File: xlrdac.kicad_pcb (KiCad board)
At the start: 2 copper layers, 99 x 99 mm, 19 parts, among them J1 Screw_Terminal_01x01, J2 Right Output, J3 Left Output, J4 Audio Stereo Input, U1 THAT1646, U2 THAT1646

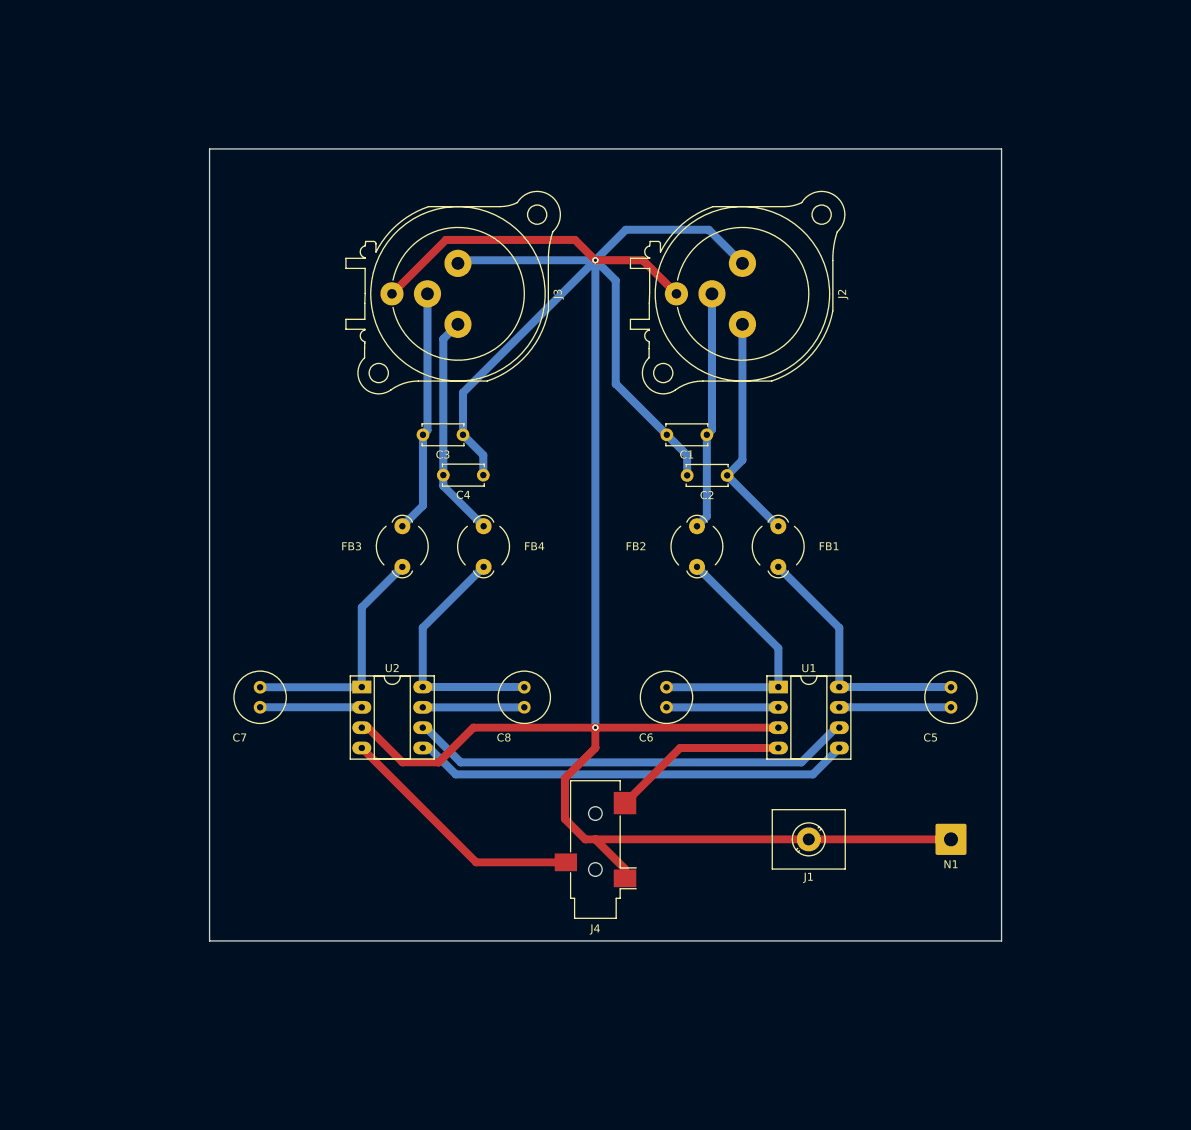
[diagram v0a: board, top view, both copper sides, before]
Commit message: Rework grounding, export side view
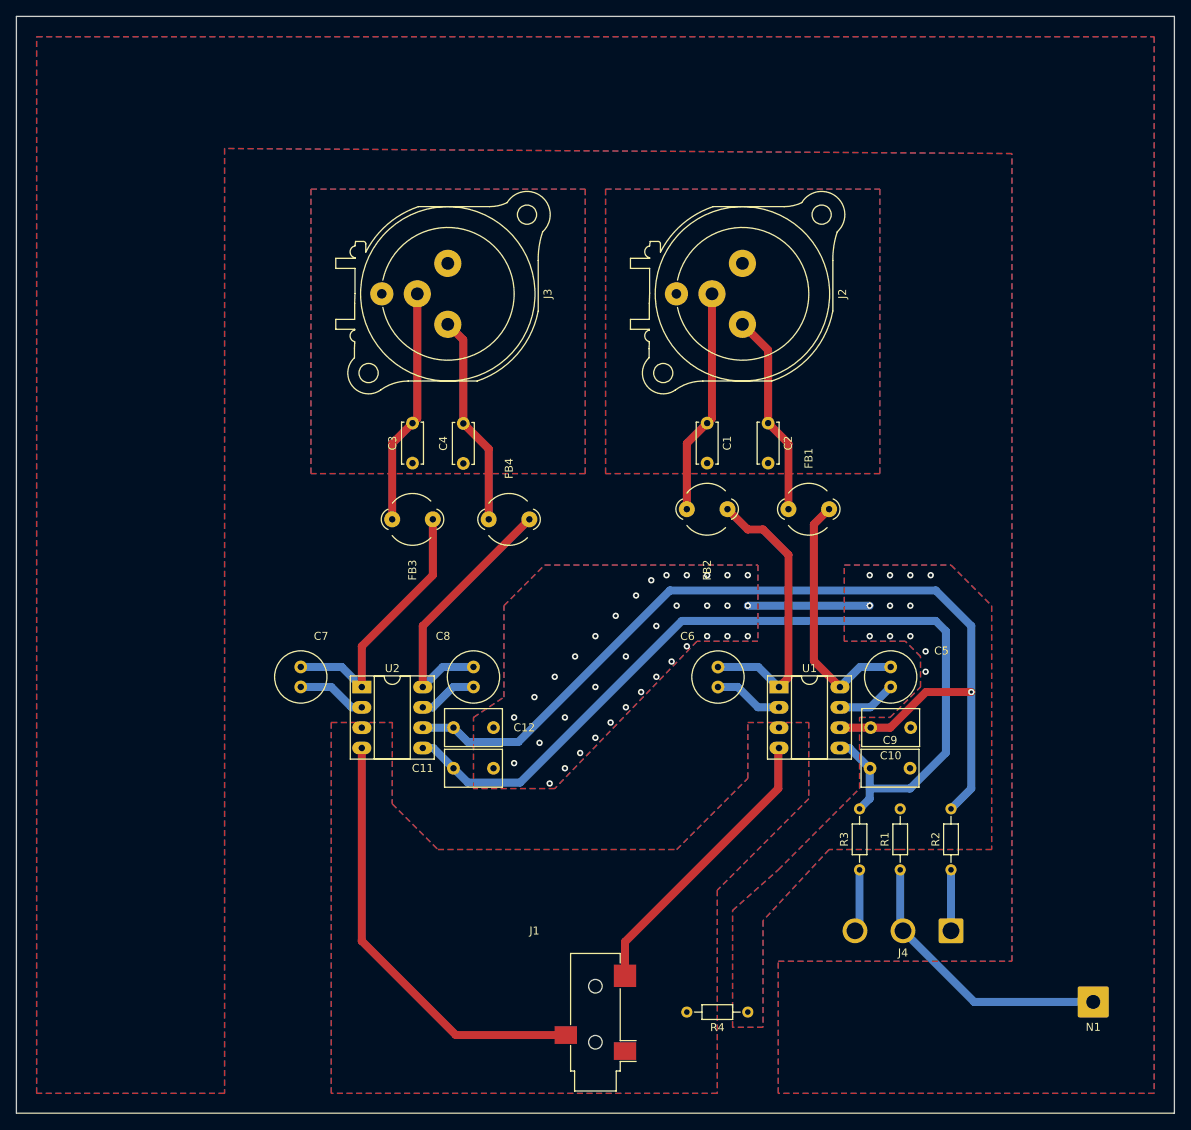
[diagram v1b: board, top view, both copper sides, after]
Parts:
- added C10: 100nF, Capacitor_THT:C_Rect_L7.0mm_W4.5mm_P5.00mm, F.Cu at (137.2, 125.7)
- added C11: 100nF, Capacitor_THT:C_Rect_L7.0mm_W4.5mm_P5.00mm, F.Cu at (80.0, 130.8)
- added C12: 100nF, Capacitor_THT:C_Rect_L7.0mm_W4.5mm_P5.00mm, F.Cu at (85.0, 125.7)
- added C9: 100nF, Capacitor_THT:C_Rect_L7.0mm_W4.5mm_P5.00mm, F.Cu at (132.1, 130.8)
- added R1: 0R, Resistor_THT:R_Axial_DIN0204_L3.6mm_D1.6mm_P7.62mm_Horizontal, F.Cu at (135.9, 143.5)
- added R2: 0R, Resistor_THT:R_Axial_DIN0204_L3.6mm_D1.6mm_P7.62mm_Horizontal, F.Cu at (142.2, 143.5)
- added R3: 0R, Resistor_THT:R_Axial_DIN0204_L3.6mm_D1.6mm_P7.62mm_Horizontal, F.Cu at (130.8, 143.5)
- added R4: 0R, Resistor_THT:R_Axial_DIN0204_L3.6mm_D1.6mm_P7.62mm_Horizontal, F.Cu at (116.8, 161.3)
- J1: value Screw_Terminal_01x01 -> StereoIn; footprint TerminalBlock_MetzConnect:TerminalBlock_MetzConnect_360271_1x01_Horizontal_ScrewM3.0_Boxed -> Connector_Audio:Jack_3.5mm_CUI_SJ-3523-SMT_Horizontal
- J2: value Right Output -> Left Output
- J3: value Left Output -> Right Output
- J4: value Audio Stereo Input -> PWR ENTRY; footprint Connector_Audio:Jack_3.5mm_CUI_SJ-3523-SMT_Horizontal -> Connector_Wire:SolderWire-1.5sqmm_1x03_P6mm_D1.7mm_OD3mm
- N1: value Housing_Pad -> CASE SHIELD
- moved J4 45.6 mm to (142.2, 151.1)
- moved J1 35.1 mm to (97.8, 162.6)
- moved N1 27.0 mm to (160.0, 160.0)
- moved FB1 9.61 mm to (127.0, 98.4), turned to 180 degrees
- moved C2 8.31 mm to (119.4, 87.7), turned to -90 degrees
- moved FB4 8.25 mm to (89.5, 99.7), turned to 180 degrees
- moved FB2 8.16 mm to (114.3, 98.4), turned to 180 degrees
- moved C5 7.96 mm to (134.7, 120.7)
- moved C3 7.24 mm to (74.9, 92.7), turned to 90 degrees
- moved FB3 7.06 mm to (77.5, 99.7), turned to 180 degrees
- moved C6 6.91 mm to (113.1, 120.7)
- moved C8 6.84 mm to (82.5, 120.7)
- moved C7 5.68 mm to (61.0, 120.7)
- moved C4 2.90 mm to (81.3, 92.7), turned to 90 degrees
- moved C1 1.46 mm to (111.8, 87.7), turned to -90 degrees
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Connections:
- C1 pad 2: Earth_Clean -> Net-(C1-Pad2)
- C2 pad 2: Earth_Clean -> Net-(C1-Pad2)
- C3 pad 1: Earth_Clean -> Net-(C3-Pad1)
- C4 pad 1: Earth_Clean -> Net-(C3-Pad1)
- J2 pad 1: Earth_Clean -> Net-(C1-Pad2)
- J2 pad G: Earth_Clean -> Net-(C1-Pad2)
- J3 pad 1: Earth_Clean -> Net-(C3-Pad1)
- J3 pad G: Earth_Clean -> Net-(C3-Pad1)
- N1 pad 1: Earth_Clean -> PWR.GND
- U1 pad 3: Earth_Clean -> GNDA
- U1 pad 4: Net-(J4-PadT) -> Net-(J1-PadT)
- U2 pad 3: Earth_Clean -> GNDA
- U2 pad 4: Net-(U2-Pad4) -> Net-(J1-PadR)
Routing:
- net Earth_Clean: track 329.4 -> 0.00 mm, vias 2 -> 0
- net VCC: track 55.7 -> 121.2 mm, vias 0 -> 1
- net VEE: track 54.8 -> 113.1 mm
- net Net-(J1-PadR): track 0.00 -> 54.5 mm
- net Net-(J1-PadT): track 0.00 -> 36.4 mm
- net PWR.GND: track 0.00 -> 35.2 mm
- net Net-(U2-Pad4): track 31.4 -> 0.00 mm
- net Net-(J4-PadT): track 22.0 -> 0.00 mm
- net GNDPWR: track 0.00 -> 15.2 mm, vias 0 -> 48
- net PWR.VEE: track 0.00 -> 7.86 mm
- net Net-(C5-Pad1): track 14.0 -> 7.40 mm
- net PWR.VCC: track 0.00 -> 6.35 mm
- net Net-(C8-Pad1): track 12.7 -> 7.40 mm
- net Net-(C6-Pad1): track 14.0 -> 8.69 mm
- net Net-(C7-Pad1): track 12.7 -> 8.69 mm
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- added copper zone on B.Cu, net GNDA
- added copper zone on F.Cu, net GNDA
- added copper zone on B.Cu, net GNDPWR
- added copper zone on F.Cu, net GNDPWR
- added copper zone on B.Cu, net Net-(C1-Pad2)
- added copper zone on F.Cu, net Net-(C1-Pad2)
- added copper zone on B.Cu, net Net-(C3-Pad1)
- added copper zone on F.Cu, net Net-(C3-Pad1)
- added copper zone on B.Cu, net PWR.GND
- added copper zone on F.Cu, net PWR.GND
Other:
- board size 99 x 99 mm -> 144.8 x 137.1 mm

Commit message: Improve ground planes
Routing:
- net GNDPWR: track 15.2 -> 24.9 mm, vias 48 -> 64
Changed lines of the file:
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@@
     (pad_to_mask_clearance 0)
     (pcbplotparams
-      (layerselection 0x00010fc_ffffffff)
+      (layerselection 0x0001000_ffffffff)
       (disableapertmacros false)
       (usegerberextensions false)
@@
       (excludeedgelayer true)
       (plotframeref false)
-      (viasonmask false)
+      (viasonmask true)
       (mode 1)
       (useauxorigin false)
@@
       (sketchpadsonfab false)
       (subtractmaskfromsilk false)
-      (outputformat 1)
+      (outputformat 4)
       (mirror false)
-      (drillshape 1)
+      (drillshape 2)
       (scaleselection 1)
-      (outputdirectory "")
+      (outputdirectory "./")
     )
   )
@@
     (fp_circle (center 6 0) (end 7.5 0) (layer "F.Fab") (width 0.1) (fill none))
     (fp_circle (center 0 0) (end 1.5 0) (layer "F.Fab") (width 0.1) (fill none))
-    (pad "1" thru_hole roundrect (at 0 0 180) (size 3.1 3.1) (drill 2.1) (layers *.Cu *.Mask) (roundrect_rratio 0.080645)
+    (pad "1" thru_hole roundrect (at 0 0 180) (size 3.1 3.1) (drill 2.1) (layers *.Cu *.Mask) (roundrect_rratio 0.08064483871)
       (net 21 "PWR.VCC") (pinfunction "Pin_1") (pintype "passive"))
     (pad "2" thru_hole circle (at 6 0 180) (size 3.1 3.1) (drill 2.1) (layers *.Cu *.Mask)
@@
   (segment (start 130.81 143.51) (end 130.81 150.56) (width 1) (layer "B.Cu") (net 22))
   (segment (start 130.81 150.56) (end 130.24 151.13) (width 1) (layer "B.Cu") (net 22))
+  (via (at 116.84 149.225) (size 0.8) (drill 0.4) (layers "F.Cu" "B.Cu") (free) (net 23))
   (via (at 93.98 124.46) (size 0.8) (drill 0.4) (layers "F.Cu" "B.Cu") (free) (net 23))
   (via (at 107.95 110.49) (size 0.8) (drill 0.4) (layers "F.Cu" "B.Cu") (free) (net 23))
   (via (at 109.22 106.68) (size 0.8) (drill 0.4) (layers "F.Cu" "B.Cu") (free) (net 23))
-  (via (at 137.16 110.49) (size 0.8) (drill 0.4) (layers "F.Cu" "B.Cu") (free) (net 23))
+  (via (at 135.89 110.49) (size 0.8) (drill 0.4) (layers "F.Cu" "B.Cu") (free) (net 23))
   (via (at 109.22 115.57) (size 0.8) (drill 0.4) (layers "F.Cu" "B.Cu") (free) (net 23))
-  (via (at 132.08 106.68) (size 0.8) (drill 0.4) (layers "F.Cu" "B.Cu") (free) (net 23))
+  (via (at 130.81 106.68) (size 0.8) (drill 0.4) (layers "F.Cu" "B.Cu") (free) (net 23))
   (via (at 116.84 114.3) (size 0.8) (drill 0.4) (layers "F.Cu" "B.Cu") (free) (net 23))
+  (via (at 116.84 152.4) (size 0.8) (drill 0.4) (layers "F.Cu" "B.Cu") (free) (net 23))
   (via (at 100.33 111.76) (size 0.8) (drill 0.4) (layers "F.Cu" "B.Cu") (free) (net 23))
+  (via (at 143.51 107.95) (size 0.8) (drill 0.4) (layers "F.Cu" "B.Cu") (free) (net 23))
   (via (at 114.3 114.3) (size 0.8) (drill 0.4) (layers "F.Cu" "B.Cu") (free) (net 23))
   (via (at 105.41 119.38) (size 0.8) (drill 0.4) (layers "F.Cu" "B.Cu") (free) (net 23))
-  (via (at 137.16 114.3) (size 0.8) (drill 0.4) (layers "F.Cu" "B.Cu") (free) (net 23))
+  (via (at 135.89 114.3) (size 0.8) (drill 0.4) (layers "F.Cu" "B.Cu") (free) (net 23))
+  (via (at 127 139.065) (size 0.8) (drill 0.4) (layers "F.Cu" "B.Cu") (free) (net 23))
   (via (at 99.695 125.095) (size 0.8) (drill 0.4) (layers "F.Cu" "B.Cu") (free) (net 23))
+  (via (at 144.78 109.22) (size 0.8) (drill 0.4) (layers "F.Cu" "B.Cu") (free) (net 23))
   (via (at 93.98 130.81) (size 0.8) (drill 0.4) (layers "F.Cu" "B.Cu") (free) (net 23))
-  (via (at 139.065 116.205) (size 0.8) (drill 0.4) (layers "F.Cu" "B.Cu") (free) (net 23))
+  (via (at 138.43 115.57) (size 0.8) (drill 0.4) (layers "F.Cu" "B.Cu") (free) (net 23))
+  (via (at 116.84 158.115) (size 0.8) (drill 0.4) (layers "F.Cu" "B.Cu") (free) (net 23))
   (via (at 106.68 106.68) (size 0.8) (drill 0.4) (layers "F.Cu" "B.Cu") (free) (net 23))
+  (via (at 124.46 141.605) (size 0.8) (drill 0.4) (layers "F.Cu" "B.Cu") (free) (net 23))
   (via (at 97.79 120.65) (size 0.8) (drill 0.4) (layers "F.Cu" "B.Cu") (free) (net 23))
+  (via (at 121.92 144.145) (size 0.8) (drill 0.4) (layers "F.Cu" "B.Cu") (free) (net 23))
   (via (at 111.76 110.49) (size 0.8) (drill 0.4) (layers "F.Cu" "B.Cu") (free) (net 23))
   (via (at 111.76 106.68) (size 0.8) (drill 0.4) (layers "F.Cu" "B.Cu") (free) (net 23))
+  (via (at 119.38 146.685) (size 0.8) (drill 0.4) (layers "F.Cu" "B.Cu") (free) (net 23))
   (via (at 87.63 130.175) (size 0.8) (drill 0.4) (layers "F.Cu" "B.Cu") (free) (net 23))
-  (via (at 132.08 110.49) (size 0.8) (drill 0.4) (layers "F.Cu" "B.Cu") (free) (net 23))
+  (via (at 133.35 139.065) (size 0.8) (drill 0.4) (layers "F.Cu" "B.Cu") (free) (net 23))
+  (via (at 130.81 110.49) (size 0.8) (drill 0.4) (layers "F.Cu" "B.Cu") (free) (net 23))
   (via (at 111.76 114.3) (size 0.8) (drill 0.4) (layers "F.Cu" "B.Cu") (free) (net 23))
   (via (at 101.6 116.84) (size 0.8) (drill 0.4) (layers "F.Cu" "B.Cu") (free) (net 23))
   (via (at 101.6 123.19) (size 0.8) (drill 0.4) (layers "F.Cu" "B.Cu") (free) (net 23))
   (via (at 97.79 114.3) (size 0.8) (drill 0.4) (layers "F.Cu" "B.Cu") (free) (net 23))
-  (via (at 134.62 114.3) (size 0.8) (drill 0.4) (layers "F.Cu" "B.Cu") (free) (net 23))
+  (via (at 133.35 114.3) (size 0.8) (drill 0.4) (layers "F.Cu" "B.Cu") (free) (net 23))
   (via (at 87.63 124.46) (size 0.8) (drill 0.4) (layers "F.Cu" "B.Cu") (free) (net 23))
+  (via (at 116.84 155.575) (size 0.8) (drill 0.4) (layers "F.Cu" "B.Cu") (free) (net 23))
   (via (at 95.885 128.905) (size 0.8) (drill 0.4) (layers "F.Cu" "B.Cu") (free) (net 23))
   (via (at 95.25 116.84) (size 0.8) (drill 0.4) (layers "F.Cu" "B.Cu") (free) (net 23))
-  (via (at 132.08 114.3) (size 0.8) (drill 0.4) (layers "F.Cu" "B.Cu") (free) (net 23))
+  (via (at 130.81 114.3) (size 0.8) (drill 0.4) (layers "F.Cu" "B.Cu") (free) (net 23))
   (via (at 92.075 132.715) (size 0.8) (drill 0.4) (layers "F.Cu" "B.Cu") (free) (net 23))
   (via (at 102.87 109.22) (size 0.8) (drill 0.4) (layers "F.Cu" "B.Cu") (free) (net 23))
-  (via (at 139.065 118.745) (size 0.8) (drill 0.4) (layers "F.Cu" "B.Cu") (free) (net 23))
+  (via (at 139.065 118.11) (size 0.8) (drill 0.4) (layers "F.Cu" "B.Cu") (free) (net 23))
+  (via (at 138.43 110.49) (size 0.8) (drill 0.4) (layers "F.Cu" "B.Cu") (free) (net 23))
+  (via (at 137.16 128.27) (size 0.8) (drill 0.4) (layers "F.Cu" "B.Cu") (free) (net 23))
   (via (at 116.84 106.68) (size 0.8) (drill 0.4) (layers "F.Cu" "B.Cu") (free) (net 23))
+  (via (at 139.065 139.065) (size 0.8) (drill 0.4) (layers "F.Cu" "B.Cu") (free) (net 23))
   (via (at 103.505 121.285) (size 0.8) (drill 0.4) (layers "F.Cu" "B.Cu") (free) (net 23))
-  (via (at 134.62 106.68) (size 0.8) (drill 0.4) (layers "F.Cu" "B.Cu") (free) (net 23))
-  (via (at 134.62 110.49) (size 0.8) (drill 0.4) (layers "F.Cu" "B.Cu") (free) (net 23))
+  (via (at 133.35 106.68) (size 0.8) (drill 0.4) (layers "F.Cu" "B.Cu") (free) (net 23))
+  (via (at 133.35 110.49) (size 0.8) (drill 0.4) (layers "F.Cu" "B.Cu") (free) (net 23))
+  (via (at 142.24 132.08) (size 0.8) (drill 0.4) (layers "F.Cu" "B.Cu") (free) (net 23))
   (via (at 97.79 127) (size 0.8) (drill 0.4) (layers "F.Cu" "B.Cu") (free) (net 23))
   (via (at 105.41 113.03) (size 0.8) (drill 0.4) (layers "F.Cu" "B.Cu") (free) (net 23))
   (via (at 114.3 106.68) (size 0.8) (drill 0.4) (layers "F.Cu" "B.Cu") (free) (net 23))
-  (via (at 137.16 106.68) (size 0.8) (drill 0.4) (layers "F.Cu" "B.Cu") (free) (net 23))
+  (via (at 135.89 106.68) (size 0.8) (drill 0.4) (layers "F.Cu" "B.Cu") (free) (net 23))
+  (via (at 145.415 139.065) (size 0.8) (drill 0.4) (layers "F.Cu" "B.Cu") (free) (net 23))
   (via (at 114.3 110.49) (size 0.8) (drill 0.4) (layers "F.Cu" "B.Cu") (free) (net 23))
   (via (at 92.71 119.38) (size 0.8) (drill 0.4) (layers "F.Cu" "B.Cu") (free) (net 23))
@@
   (via (at 107.315 117.475) (size 0.8) (drill 0.4) (layers "F.Cu" "B.Cu") (free) (net 23))
   (via (at 116.84 110.49) (size 0.8) (drill 0.4) (layers "F.Cu" "B.Cu") (free) (net 23))
-  (via (at 139.7 106.68) (size 0.8) (drill 0.4) (layers "F.Cu" "B.Cu") (free) (net 23))
-  (segment (start 116.84 110.49) (end 132.08 110.49) (width 1) (layer "B.Cu") (net 23))
+  (via (at 138.43 106.68) (size 0.8) (drill 0.4) (layers "F.Cu" "B.Cu") (free) (net 23))
+  (segment (start 139.065 126.365) (end 139.065 118.11) (width 1) (layer "B.Cu") (net 23))
+  (segment (start 137.16 128.27) (end 139.065 126.365) (width 1) (layer "B.Cu") (net 23))
+  (segment (start 116.84 110.49) (end 130.81 110.49) (width 1) (layer "B.Cu") (net 23))
   (zone (net 23) (net_name "GNDPWR") (layers F&B.Cu) (hatch edge 0.508)
     (connect_pads (clearance 1))
@@
         (xy 114.935 163.195)
         (xy 114.935 148.59)
-        (xy 120.65 143.51)
-        (xy 130.81 133.35)
-        (xy 130.81 124.46)
+        (xy 127.635 135.89)
+        (xy 132.08 135.89)
+        (xy 134.62 132.715)
         (xy 134.62 124.46)
         (xy 138.43 120.65)
